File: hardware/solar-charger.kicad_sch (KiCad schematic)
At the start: 23 parts, among them J1 Conn_01x02_Male, J2 ISENSE_SOLAR, J3 ISENSE_SOLAR, J4 ISENSE_SOLAR, J5 ISENSE_DISCHARGE, J6 Conn_01x02_Male, Q1 AOI21357, Q2 AOI21357, Q3 AOI21357, Q4 AOI21357, U1 MCP6002-xP

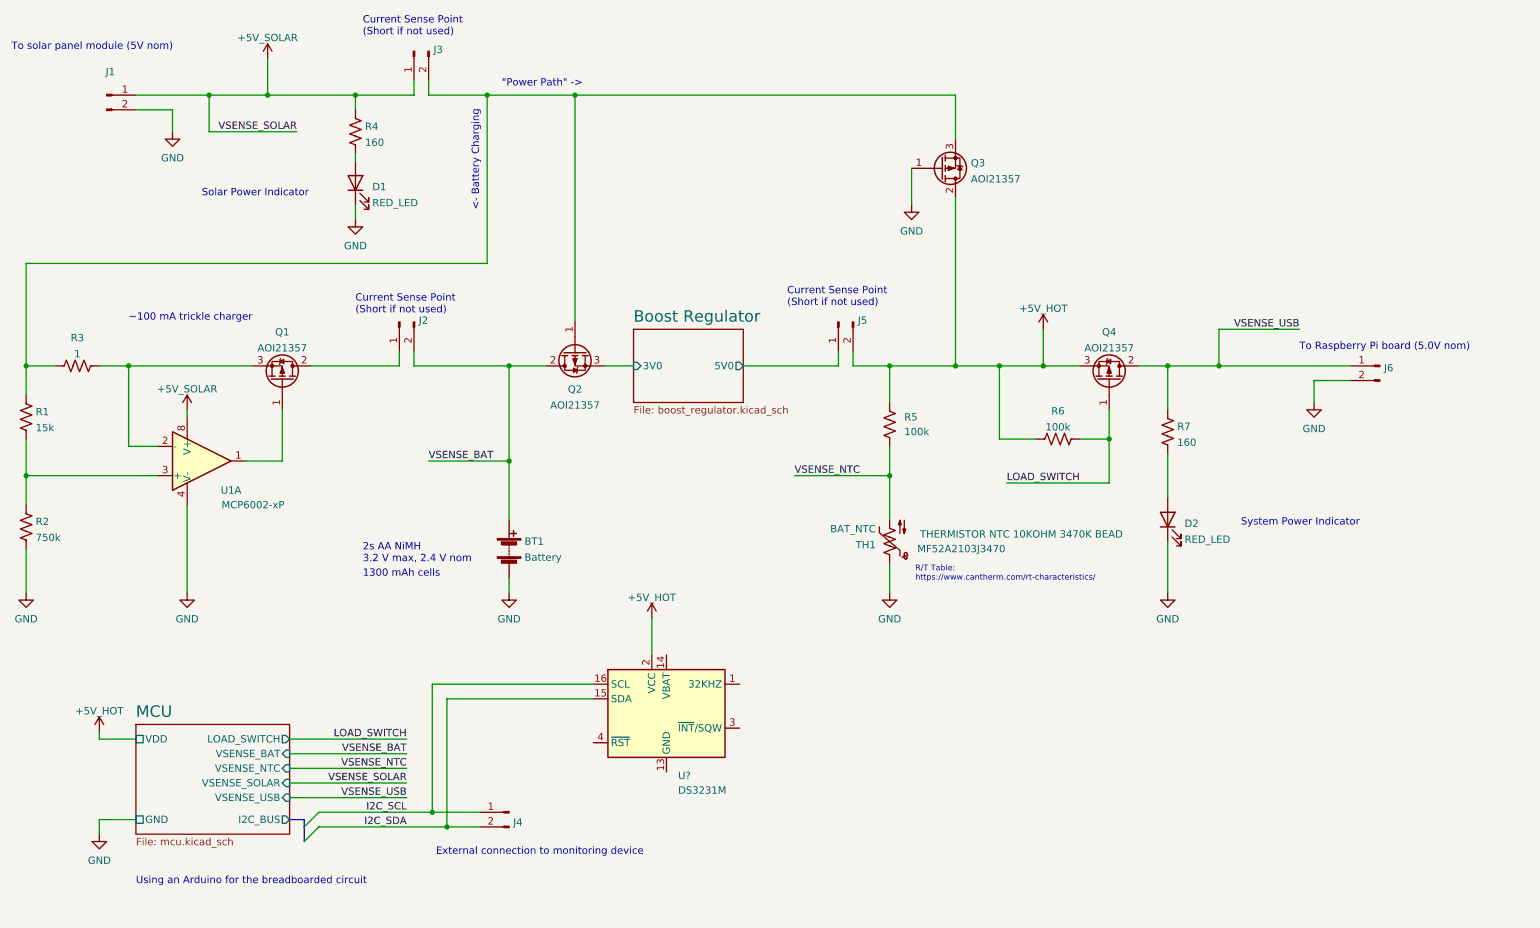
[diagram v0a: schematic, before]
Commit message: hardware: Replace power path MOSFET with Schottky
MOSFET has a reverse leakage current over the body diode, which brings
voltage back onto the `5V_SOLAR` net, turning off Q2. We want `5V_SOLAR`
to be near 0V to ensure that Q2 turns on well. Therefore, we need to use
a diode here to block the reverse leakage current. A Schottky has a low
voltage drop so seems like an appropriate choice. Further improvement
may be made with a ideal diode solution.
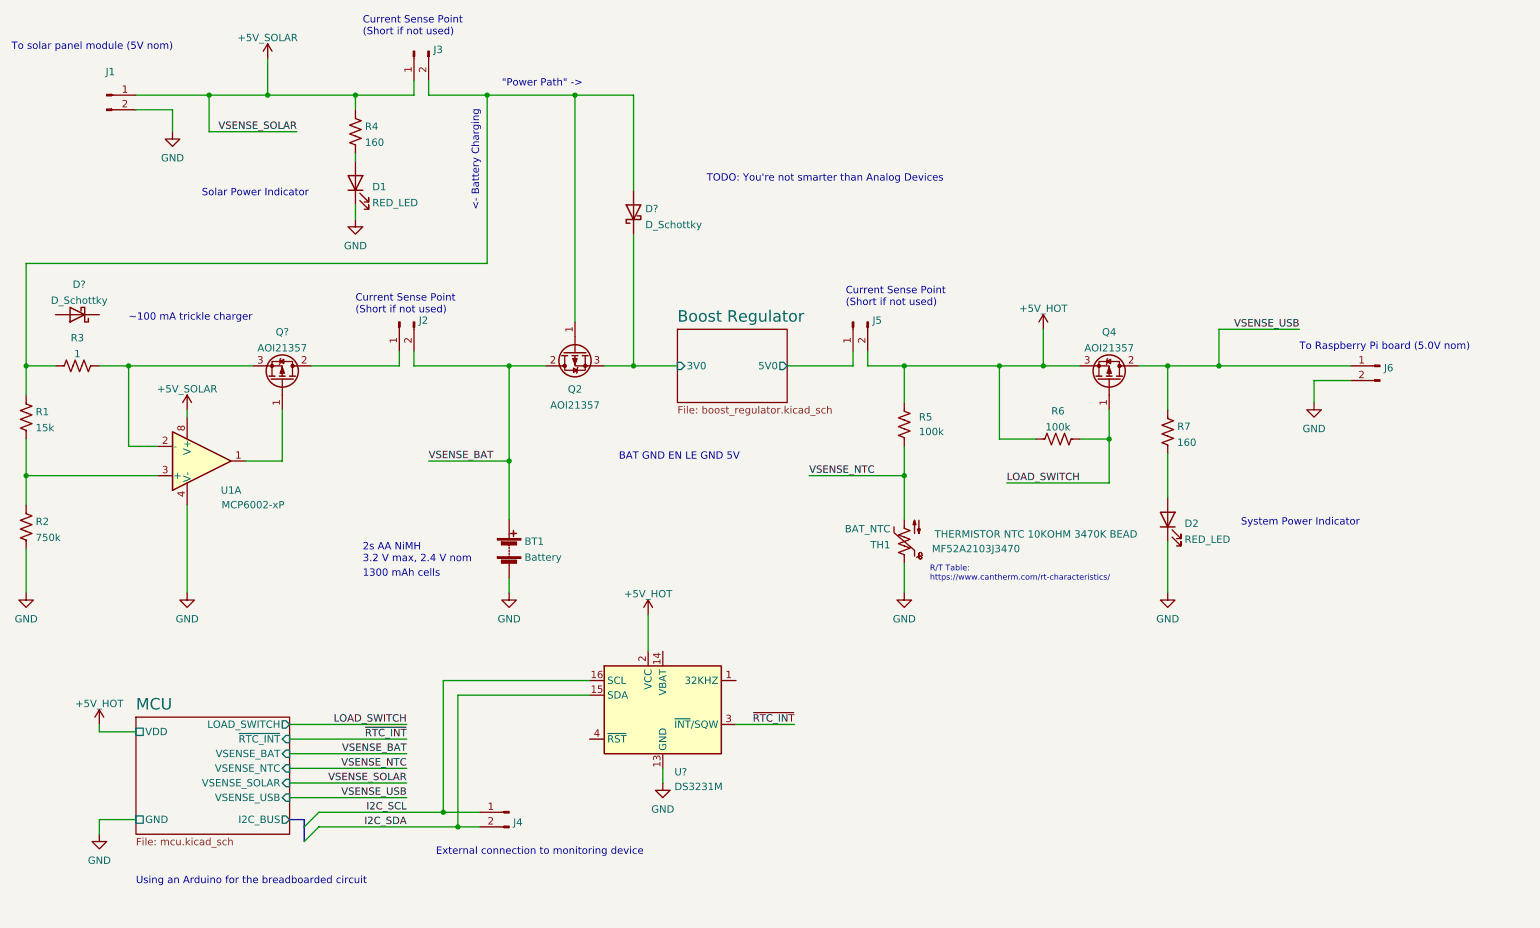
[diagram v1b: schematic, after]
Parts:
- removed Q1, Q3: AOI21357, symbol Device:Q_PMOS_GDS
- added D? (x2): D_Schottky, symbol Device:D_Schottky
- added Q?: AOI21357, symbol Device:Q_PMOS_GDS
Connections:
- net Boost Regulator/3V0: now also D?.1 (K)
- net GND: now also U?.10 (GND), U?.11 (GND), U?.12 (GND), U?.13 (GND), U?.5 (GND), U?.6 (GND), U?.7 (GND), U?.8 (GND), U?.9 (GND)
- net at U1.1: now also Q?.1 (G)
- net at J2.1 (Pin_1): now also Q?.2 (D)
- net at R3.2, U1.2 (-): now also Q?.3 (S)
- net at J3.2 (Pin_2), Q2.1 (G), R1.1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: now also D?.2 (A)
- net ~{RTC_INT}: now reaches U?.3 (~{INT}/SQW)
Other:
- sheet MCU ports: added ~{RTC_INT}; removed none
- note added: "BAT GND EN LE GND 5V"
- note added: "TODO: You're not smarter than Analog Devices"
- moved on the sheet: J5, R5, TH1, U?

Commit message: hardware: Add Q2 to prevent discharging battery from 5V_SOLAR net, misc cleanup
The body diode of Q1 allowed current to be conducted back into the solar
panel. This is something that can happen during the night in a typical
solar panel circuit. I don't know what our solar panel module looks like
internally so add this just in case.
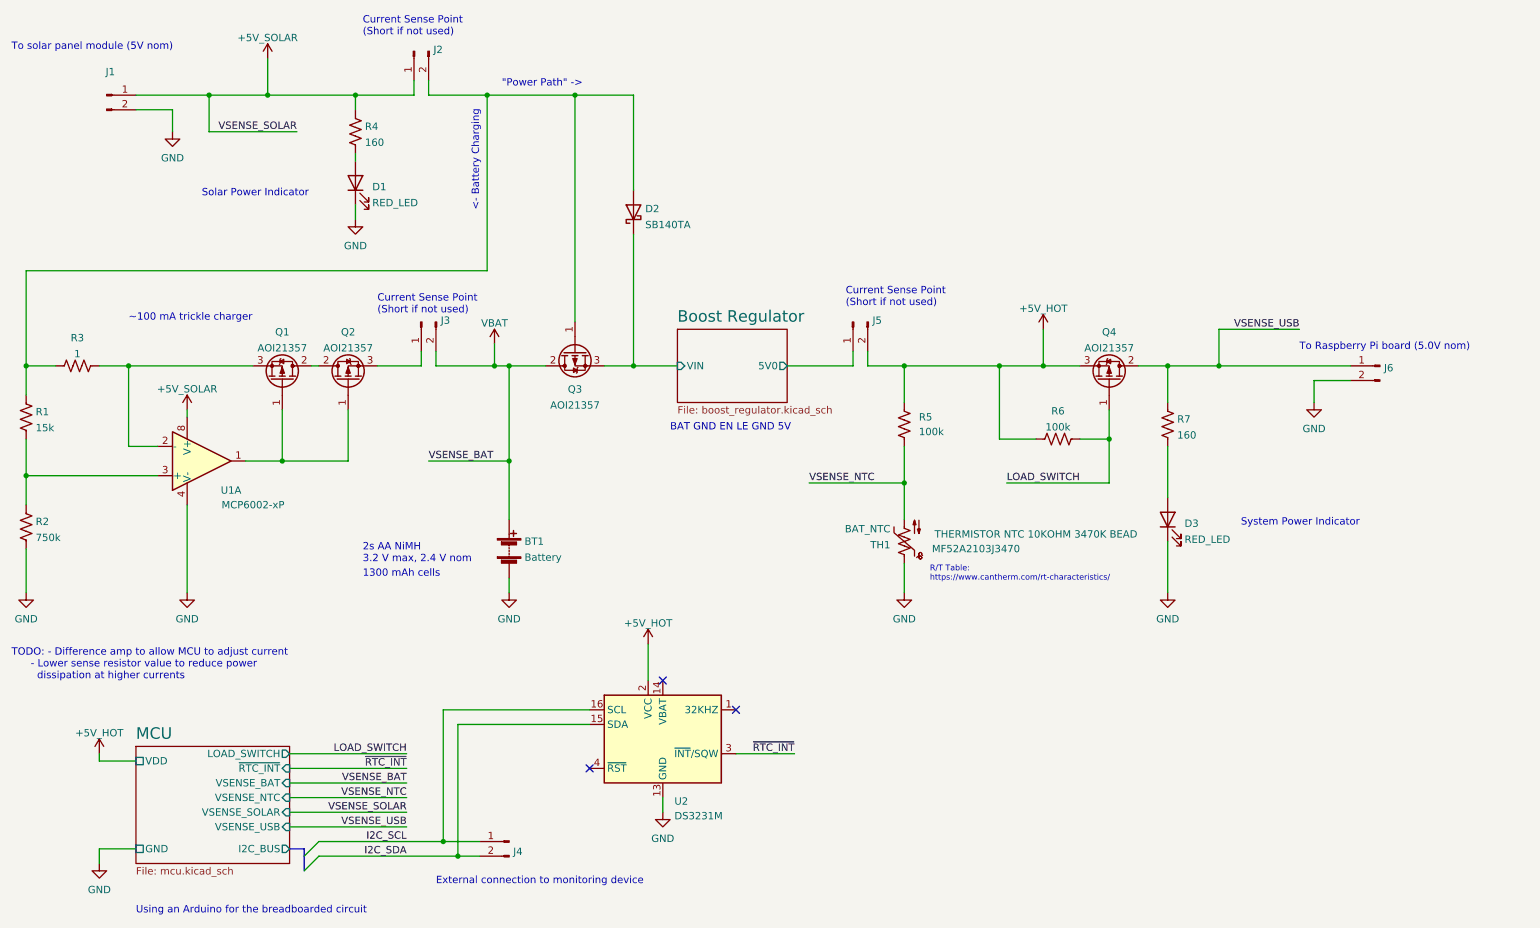
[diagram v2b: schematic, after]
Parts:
- removed D?: D_Schottky, symbol Device:D_Schottky
- removed Q?: AOI21357, symbol Device:Q_PMOS_GDS
- added Q1, Q2: AOI21357, symbol Device:Q_PMOS_GDS
- D2: renamed from D?; value D_Schottky -> SB140TA
- gave numbers to parts that had none: 1
- renumbered D2 to D3, J3 to J2, J2 to J3, Q2 to Q3
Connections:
- net at J3.1 (Pin_1): now also Q2.3 (S)
- net at U1.1: now also Q1.1 (G), Q2.1 (G)
- net at R3.2, U1.2 (-): now also Q1.3 (S)
- net Boost Regulator/3V0 renamed Boost Regulator/VIN
- net VSENSE_BAT renamed VDD
- new net: Q1.2 (D), Q2.2 (D)
- no-connect marks 0 -> 3
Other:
- sheet Boost Regulator ports: added VIN; removed 3V0
- note added: "TODO: - Difference amp to allow MCU to adjust current - Lower sense resistor value to reduce power dissipation at higher currents"
- note removed: "TODO: You're not smarter than Analog Devices"
- moved on the sheet: J3, J4, R7, U2
